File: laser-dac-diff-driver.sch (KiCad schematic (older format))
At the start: 13 parts, among them P101 CONN_2, P102 CONN_3X2, P103 CONN_6X2, U101 AD5689RARUZ, U102 74HC04

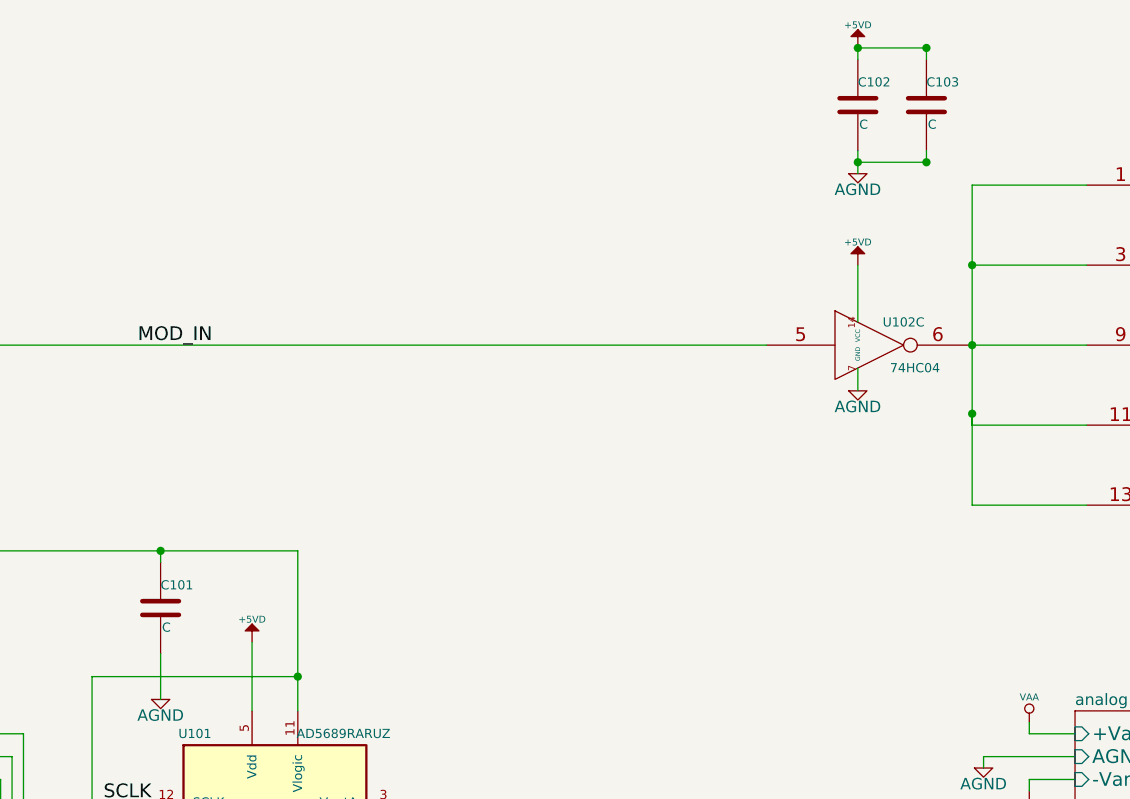
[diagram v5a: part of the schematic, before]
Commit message: Added bill of materials (shouldn't REALLY be any non-bom changes??)
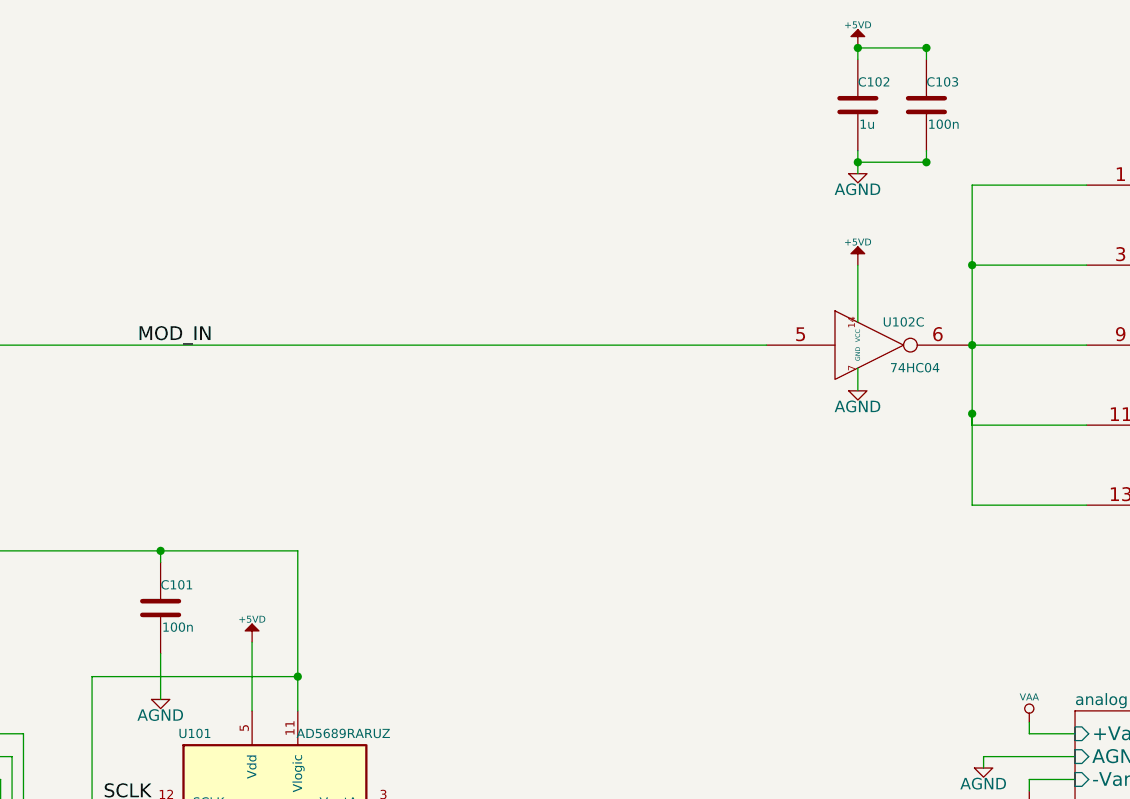
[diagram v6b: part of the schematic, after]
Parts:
- C101, C103: value C -> 100n
- C102: value C -> 1u
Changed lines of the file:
@@
 P 3850 3150
 F 0 "C101" H 3850 3250 40  0000 L CNN
-F 1 "C" H 3856 3065 40  0000 L CNN
+F 1 "100n" H 3856 3065 40  0000 L CNN
 F 2 "" H 3888 3000 30  0000 C CNN
 F 3 "" H 3850 3150 60  0000 C CNN
@@
 P 6900 950
 F 0 "C102" H 6900 1050 40  0000 L CNN
-F 1 "C" H 6906 865 40  0000 L CNN
+F 1 "1u" H 6906 865 40  0000 L CNN
 F 2 "" H 6938 800 30  0000 C CNN
 F 3 "" H 6900 950 60  0000 C CNN
@@
 P 7200 950
 F 0 "C103" H 7200 1050 40  0000 L CNN
-F 1 "C" H 7206 865 40  0000 L CNN
+F 1 "100n" H 7206 865 40  0000 L CNN
 F 2 "" H 7238 800 30  0000 C CNN
 F 3 "" H 7200 950 60  0000 C CNN
